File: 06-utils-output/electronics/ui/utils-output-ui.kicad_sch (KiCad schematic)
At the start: 32 parts, among them J1 Conn_02x03_Odd_Even, J2 Conn_02x04_Odd_Even, J3 Conn_02x02_Odd_Even, J4 Conn_01x02, J5 Conn_01x06, J6 Conn_02x05_Odd_Even, Q1 2N3904

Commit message: Utils+output PCB connectors positions checked
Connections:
- net OUTPUT_OUT: now also J_MAIN_OUT1.TN
- net OUTPUT_OUT_DEFAULT: no longer names the net of J5.3 (Pin_3)
- net OUTPUT_OUT_DEFAULT: no longer J_MAIN_OUT1.TN
- no-connect marks 6 -> 7
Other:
- note added: "Dual mono out"
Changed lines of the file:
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@@
 		(company "Shmøergh")
+	)
+	(text "Dual mono out"
+		(exclude_from_sim no)
+		(at 186.69 120.65 0)
+		(effects
+			(font
+				(size 1.27 1.27)
+			)
+		)
 	)
 	(text "UI power connection"
@@
 	)
 	(junction
+		(at 180.34 115.57)
+		(diameter 0)
+		(color 0 0 0 0)
+	)
+	(junction
 		(at 52.07 185.42)
 		(diameter 0)
@@
 	)
 	(no_connect
+		(at 242.57 34.29)
+	)
+	(no_connect
 		(at 252.73 102.87)
 	)
@@
 	(wire
 		(pts
+			(xy 180.34 115.57) (xy 185.42 115.57)
+		)
+		(stroke
+			(width 0)
+			(type default)
+		)
+	)
+	(wire
+		(pts
 			(xy 115.57 176.53) (xy 115.57 173.99)
 		)
@@
 	(wire
 		(pts
-			(xy 240.03 34.29) (xy 242.57 34.29)
-		)
-		(stroke
-			(width 0)
-			(type default)
-		)
-	)
-	(wire
-		(pts
 			(xy 48.26 182.88) (xy 48.26 180.34)
 		)
@@
 	(wire
 		(pts
+			(xy 180.34 115.57) (xy 180.34 118.11)
+		)
+		(stroke
+			(width 0)
+			(type default)
+		)
+	)
+	(wire
+		(pts
 			(xy 66.04 180.34) (xy 48.26 180.34)
 		)
@@
 			(width 0)
 			(type default)
-		)
-	)
-	(global_label "OUTPUT_OUT_DEFAULT"
-		(shape input)
-		(at 240.03 34.29 180)
-		(fields_autoplaced yes)
-		(effects
-			(font
-				(size 1.27 1.27)
-			)
-			(justify right)
-		)
-		(property "Intersheetrefs" "${INTERSHEET_REFS}"
-			(at 216.3619 34.29 0)
-			(effects
-				(font
-					(size 1.27 1.27)
-				)
-				(justify right)
-				(hide yes)
-			)
 		)
 	)
@@
 	(global_label "OUTPUT_OUT"
 		(shape output)
-		(at 180.34 115.57 0)
-		(fields_autoplaced yes)
-		(effects
-			(font
-				(size 1.27 1.27)
-			)
-			(justify left)
-		)
-		(property "Intersheetrefs" "${INTERSHEET_REFS}"
-			(at 195.1181 115.57 0)
+		(at 185.42 115.57 0)
+		(fields_autoplaced yes)
+		(effects
+			(font
+				(size 1.27 1.27)
+			)
+			(justify left)
+		)
+		(property "Intersheetrefs" "${INTERSHEET_REFS}"
+			(at 200.1981 115.57 0)
 			(effects
 				(font
@@
 			(effects
 				(font
-					(size 1.27 1.27)
-				)
-				(justify left)
-				(hide yes)
-			)
-		)
-	)
-	(global_label "OUTPUT_OUT_DEFAULT"
-		(shape input)
-		(at 180.34 118.11 0)
-		(fields_autoplaced yes)
-		(effects
-			(font
-				(size 1.27 1.27)
-			)
-			(justify left)
-		)
-		(property "Intersheetrefs" "${INTERSHEET_REFS}"
-			(at 204.0081 118.11 0)
-			(effects
-				(font

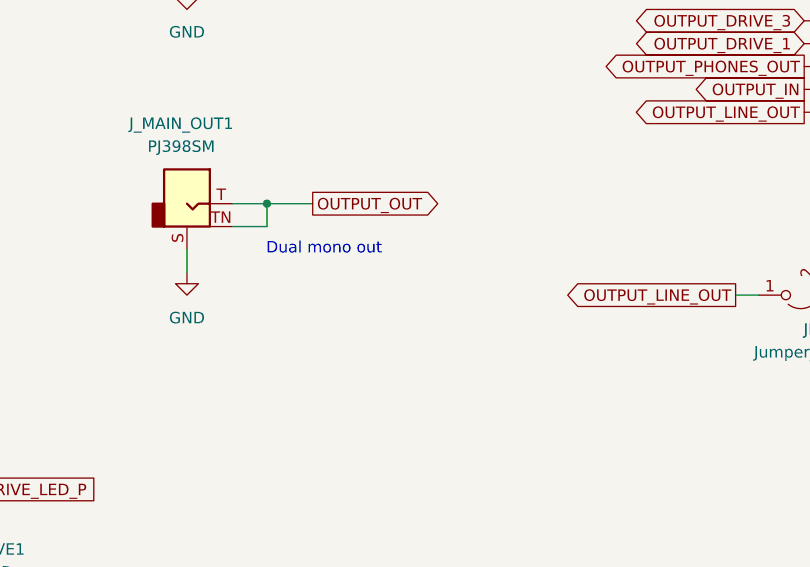
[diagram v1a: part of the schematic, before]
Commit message: Added production files for Utils+output
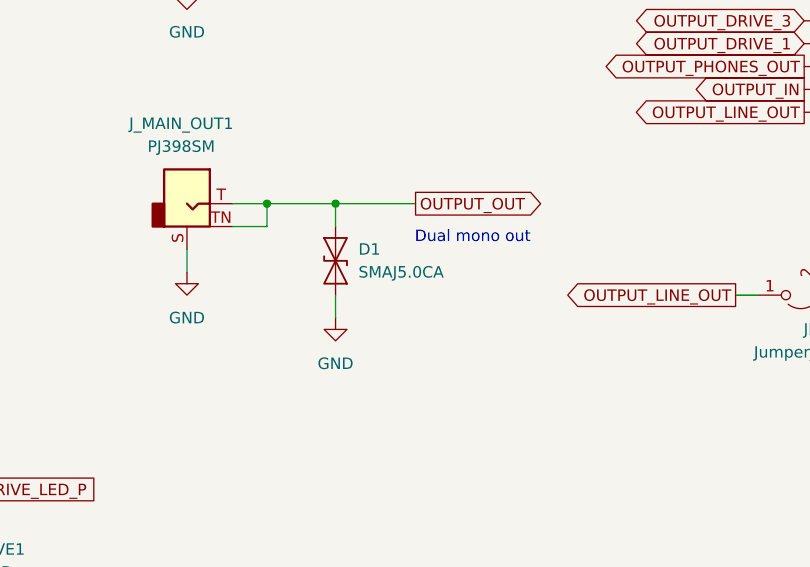
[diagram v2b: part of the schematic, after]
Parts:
- added D1: SMAJ5.0CA, Diode_SMD:D_SMA, symbol Diode:SMAJ5.0CA
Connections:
- net GND: now also D1.1 (A1)
- net OUTPUT_OUT: now also D1.2 (A2)
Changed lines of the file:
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@@
 	(text "Dual mono out"
 		(exclude_from_sim no)
-		(at 186.69 120.65 0)
+		(at 203.2 119.38 0)
 		(effects
 			(font
@@
 	)
 	(junction
+		(at 187.96 115.57)
+		(diameter 0)
+		(color 0 0 0 0)
+	)
+	(junction
 		(at 48.26 180.34)
 		(diameter 0)
@@
 	(wire
 		(pts
+			(xy 187.96 115.57) (xy 196.85 115.57)
+		)
+		(stroke
+			(width 0)
+			(type default)
+		)
+	)
+	(wire
+		(pts
 			(xy 52.07 187.96) (xy 52.07 185.42)
 		)
@@
 	(wire
 		(pts
-			(xy 180.34 115.57) (xy 185.42 115.57)
+			(xy 180.34 115.57) (xy 187.96 115.57)
 		)
 		(stroke
@@
 	(wire
 		(pts
+			(xy 187.96 128.27) (xy 187.96 125.73)
+		)
+		(stroke
+			(width 0)
+			(type default)
+		)
+	)
+	(wire
+		(pts
 			(xy 105.41 130.81) (xy 105.41 133.35)
 		)
@@
 	(wire
 		(pts
+			(xy 187.96 115.57) (xy 187.96 118.11)
+		)
+		(stroke
+			(width 0)
+			(type default)
+		)
+	)
+	(wire
+		(pts
 			(xy 240.03 36.83) (xy 242.57 36.83)
 		)
@@
 	(global_label "OUTPUT_OUT"
 		(shape output)
-		(at 185.42 115.57 0)
+		(at 196.85 115.57 0)
 		(fields_autoplaced yes)
 		(effects
@@
 		)
 		(property "Intersheetrefs" "${INTERSHEET_REFS}"
-			(at 200.1981 115.57 0)
+			(at 211.6281 115.57 0)
 			(effects
 				(font
@@
 	)
 	(symbol
+		(lib_id "power:GND")
+		(at 187.96 128.27 0)
+		(unit 1)
+		(exclude_from_sim no)
+		(in_bom yes)
+		(on_board yes)
+		(dnp no)
+		(fields_autoplaced yes)
+		(property "Reference" "#PWR020"
+			(at 187.96 134.62 0)
+			(effects
+				(font
+					(size 1.27 1.27)
+				)
+				(hide yes)
+			)
+		)
+		(property "Value" "GND"
+			(at 187.96 133.35 0)
+			(effects
+				(font
+					(size 1.27 1.27)
+				)
+			)
+		)
+		(property "Footprint" ""
+			(at 187.96 128.27 0)
+			(effects
+				(font
+					(size 1.27 1.27)
+				)
+				(hide yes)
+			)
+		)
+		(property "Datasheet" ""
+			(at 187.96 128.27 0)
+			(effects
+				(font
+					(size 1.27 1.27)
+				)
+				(hide yes)
+			)
+		)
+		(property "Description" "Power symbol creates a global label with name \"GND\" , ground"
+			(at 187.96 128.27 0)
+			(effects
+				(font
+					(size 1.27 1.27)
+				)
+				(hide yes)
+			)
+		)
+		(pin "1"
+		)
+		(instances
+			(project ""
+				(path "/ab333f71-eefa-415f-b212-ebe7a942b1c8"
+					(reference "#PWR020")
+					(unit 1)
+				)
+			)
+		)
+	)
+	(symbol
 		(lib_id "Connector_Generic:Conn_01x02")
 		(at 30.48 152.4 0)
@@
 					(unit 1)
 				)
+			)
+		)
+	)
+	(symbol
+		(lib_id "Diode:SMAJ5.0CA")
+		(at 187.96 121.92 90)
+		(unit 1)
+		(exclude_from_sim no)
+		(in_bom yes)
+		(on_board yes)
+		(dnp no)
+		(fields_autoplaced yes)
+		(property "Reference" "D1"
+			(at 190.5 120.6499 90)
+			(effects
+				(font
+					(size 1.27 1.27)
+				)
+				(justify right)
+			)
+		)
+		(property "Value" "SMAJ5.0CA"
+			(at 190.5 123.1899 90)
+			(effects
+				(font
+					(size 1.27 1.27)
+				)
+				(justify right)
+			)
+		)
+		(property "Footprint" "Diode_SMD:D_SMA"
+			(at 193.04 121.92 0)
+			(effects
+				(font
+					(size 1.27 1.27)
+				)
+				(hide yes)
+			)
+		)
+		(property "Datasheet" "https://www.littelfuse.com/media?resourcetype=datasheets&itemid=75e32973-b177-4ee3-a0ff-cedaf1abdb93&filename=smaj-datasheet"
+			(at 187.96 121.92 0)
+			(effects
+				(font
+					(size 1.27 1.27)
+				)
+				(hide yes)
+			)
+		)
+		(property "Description" "400W bidirectional Transient Voltage Suppressor, 5.0Vr, SMA(DO-214AC)"
+			(at 187.96 121.92 0)
+			(effects
+				(font
+					(size 1.27 1.27)
+				)
+				(hide yes)
+			)
+		)
+		(pin "1"
+		)
+		(pin "2"
+		)
+		(instances
+			(project ""
+				(path "/ab333f71-eefa-415f-b212-ebe7a942b1c8"
+					(reference "D1")
+					(unit 1)
+				)

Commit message: Updated LFO LED resistor value
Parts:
- R2: value 1k -> 4.7k
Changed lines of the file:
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@@
 			)
 		)
-		(property "Value" "1k"
+		(property "Value" "4.7k"
 			(at 118.11 160.0199 0)
 			(effects
